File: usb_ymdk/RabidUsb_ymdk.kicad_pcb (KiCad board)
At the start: 2 copper layers, 40.6 x 16.8 mm, 18 parts, among them J1 USB_C_Receptacle_USB2.0, J2 Conn_01x04, U1 SRV05-4

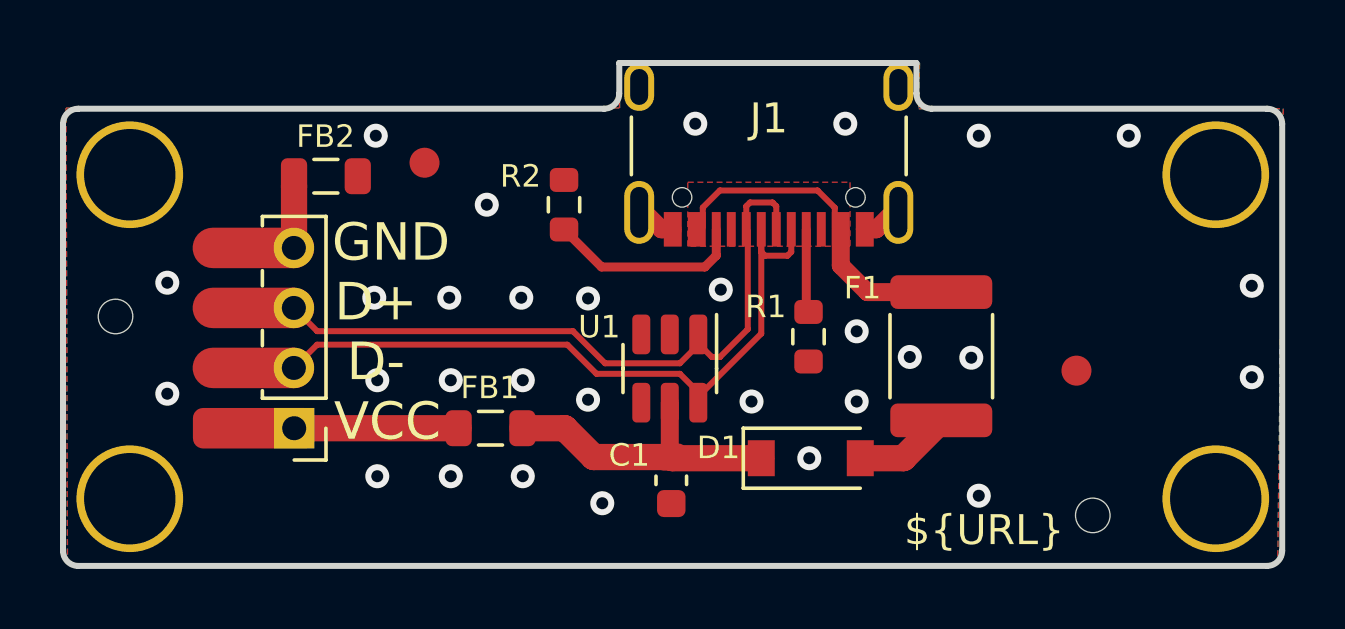
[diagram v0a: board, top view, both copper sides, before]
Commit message: USB: Move usb_ymdk holes up a couple thou.
This should helpfully give some more room, so the board isn't such a
tight fit in the YMDK F87 case.
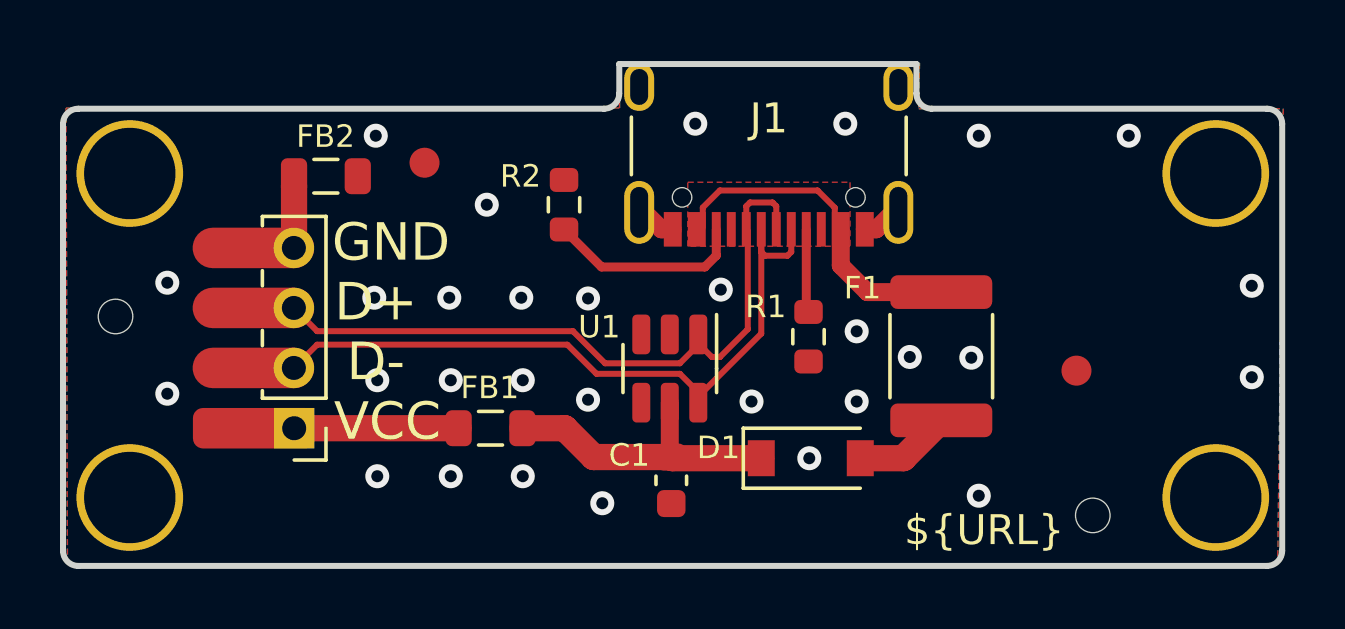
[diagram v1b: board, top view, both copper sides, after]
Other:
- board size 40.6 x 16.8 mm -> 40.6 x 16.7 mm
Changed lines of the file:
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@@
   )
   (footprint "ymdk_footprints:MountingHole_.12in_Pad_.02in" (layer "F.Cu")
-    (at 147.9 55.7)
+    (at 147.9 55.66)
     (descr "Mounting Hole 2.5mm")
     (tags "mounting hole 2.5mm")
@@
     (fp_circle (center 0 0) (end 2.032 0) (layer "F.CrtYd") (width 0.05) (fill none))
     (pad "1" thru_hole circle (at 0 0) (size 3.556 3.556) (drill 3.048) (layers *.Cu *.Mask)
-      (net 2 "GND") (pinfunction "1") (pintype "input"))
+      (net 2 "GND") (pinfunction "1") (pintype "input") (zone_connect 2))
   )
   (footprint "Resistor_SMD:R_0603_1608Metric" (layer "F.Cu")
@@
   )
   (footprint "ymdk_footprints:MountingHole_.12in_Pad_.02in" (layer "F.Cu")
-    (at 111.7 55.7)
+    (at 111.7 55.66)
     (descr "Mounting Hole 2.5mm")
     (tags "mounting hole 2.5mm")
@@
     (fp_circle (center 0 0) (end 2.032 0) (layer "F.CrtYd") (width 0.05) (fill none))
     (pad "1" thru_hole circle (at 0 0) (size 3.556 3.556) (drill 3.048) (layers *.Cu *.Mask)
-      (net 2 "GND") (pinfunction "1") (pintype "input"))
+      (net 2 "GND") (pinfunction "1") (pintype "input") (zone_connect 2))
   )
   (footprint "ymdk_footprints:MountingHole_.12in_Pad_.02in" (layer "F.Cu")
-    (at 147.9 66.5)
+    (at 147.9 66.46)
     (descr "Mounting Hole 2.5mm")
     (tags "mounting hole 2.5mm")
@@
     (fp_circle (center 0 0) (end 2.032 0) (layer "F.CrtYd") (width 0.05) (fill none))
     (pad "1" thru_hole circle (at 0 0) (size 3.556 3.556) (drill 3.048) (layers *.Cu *.Mask)
-      (net 2 "GND") (pinfunction "1") (pintype "input"))
+      (net 2 "GND") (pinfunction "1") (pintype "input") (zone_connect 2))
   )
   (footprint "Fiducial:Fiducial_1mm_Mask2mm" (layer "F.Cu")
@@
   )
   (footprint "ymdk_footprints:MountingHole_.12in_Pad_.02in" (layer "F.Cu")
-    (at 111.7 66.5)
+    (at 111.7 66.46)
     (descr "Mounting Hole 2.5mm")
     (tags "mounting hole 2.5mm")
@@
     (fp_circle (center 0 0) (end 2.032 0) (layer "F.CrtYd") (width 0.05) (fill none))
     (pad "1" thru_hole circle (at 0 0) (size 3.556 3.556) (drill 3.048) (layers *.Cu *.Mask)
-      (net 2 "GND") (pinfunction "1") (pintype "input"))
+      (net 2 "GND") (pinfunction "1") (pintype "input") (zone_connect 2))
   )
   (gr_poly
@@
   (gr_line (start 150.114 68.232) (end 150.114 54.008) (layer "Edge.Cuts") (width 0.2))
   (gr_arc (start 109.982 68.74) (mid 109.62279 68.59121) (end 109.474 68.232) (layer "Edge.Cuts") (width 0.2))
-  (gr_line (start 128.016 51.976) (end 128.016 52.992) (layer "Edge.Cuts") (width 0.2))
+  (gr_line (start 128.016 52.01) (end 128.016 52.992) (layer "Edge.Cuts") (width 0.2))
   (gr_line (start 149.606 53.5) (end 138.43 53.5) (layer "Edge.Cuts") (width 0.2))
   (gr_arc (start 138.43 53.5) (mid 138.07079 53.35121) (end 137.922 52.992) (layer "Edge.Cuts") (width 0.2))
-  (gr_line (start 137.922 51.976) (end 137.922 52.992) (layer "Edge.Cuts") (width 0.2))
-  (gr_line (start 137.922 51.976) (end 128.016 51.976) (layer "Edge.Cuts") (width 0.2))
+  (gr_line (start 137.922 52.01) (end 137.922 52.992) (layer "Edge.Cuts") (width 0.2))
+  (gr_line (start 137.922 52.01) (end 128.016 52.01) (layer "Edge.Cuts") (width 0.2))
   (gr_arc (start 150.114 68.232) (mid 149.96521 68.59121) (end 149.606 68.74) (layer "Edge.Cuts") (width 0.2))
   (gr_line (start 109.474 54.008) (end 109.474 68.232) (layer "Edge.Cuts") (width 0.2))
